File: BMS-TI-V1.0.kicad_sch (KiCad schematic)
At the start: 0 parts

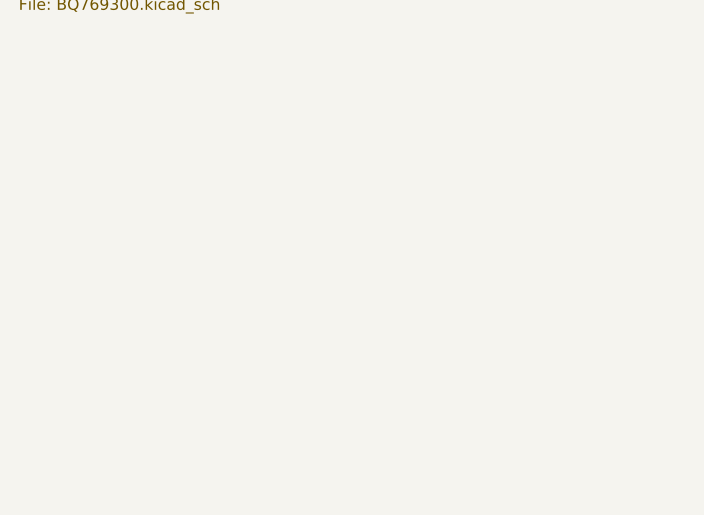
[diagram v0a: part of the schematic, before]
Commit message: Added BQ78350 Gas-gauge companion
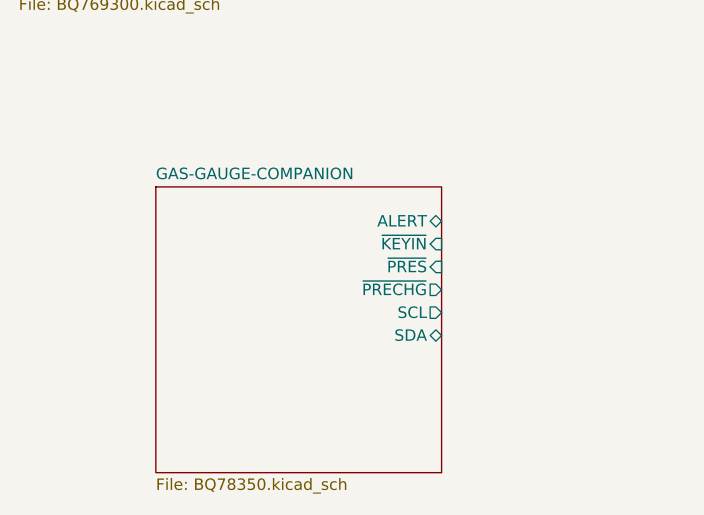
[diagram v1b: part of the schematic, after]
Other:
- added sheet GAS-GAUGE-COMPANION (BQ78350.kicad_sch)
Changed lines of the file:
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@@
+		)
+	)
+	(sheet
+		(at 120.65 129.54)
+		(size 31.75 31.75)
+		(fields_autoplaced yes)
+		(stroke
+			(width 0.1524)
+			(type solid)
+		)
+		(fill
+			(color 0 0 0 0.0000)
+		)
+		(property "Sheetname" "GAS-GAUGE-COMPANION"
+			(at 120.65 128.8284 0)
+			(effects
+				(font
+					(size 1.27 1.27)
+				)
+				(justify left bottom)
+			)
+		)
+		(property "Sheetfile" "BQ78350.kicad_sch"
+			(at 120.65 161.8746 0)
+			(effects
+				(font
+					(size 1.27 1.27)
+				)
+				(justify left top)
+			)
+		)
+		(pin "ALERT" bidirectional
+			(at 152.4 133.35 0)
+			(effects
+				(font
+					(size 1.27 1.27)
+				)
+				(justify right)
+			)
+		)
+		(pin "~{KEYIN}" input
+			(at 152.4 135.89 0)
+			(effects
+				(font
+					(size 1.27 1.27)
+				)
+				(justify right)
+			)
+		)
+		(pin "~{PRES}" input
+			(at 152.4 138.43 0)
+			(effects
+				(font
+					(size 1.27 1.27)
+				)
+				(justify right)
+			)
+		)
+		(pin "~{PRECHG}" output
+			(at 152.4 140.97 0)
+			(effects
+				(font
+					(size 1.27 1.27)
+				)
+				(justify right)
+			)
+		)
+		(pin "SCL" output
+			(at 152.4 143.51 0)
+			(effects
+				(font
+					(size 1.27 1.27)
+				)
+				(justify right)
+			)
+		)
+		(pin "SDA" bidirectional
+			(at 152.4 146.05 0)
+			(effects
+				(font
+					(size 1.27 1.27)
+				)
+				(justify right)
+			)
+		)
+		(instances
+			(project "BMS-TI-V1.0"
+				(path "/1b322c88-a1e6-4706-b5ad-2d81e9035abf"
+					(page "4")
+				)
+			)
 		)
 	)

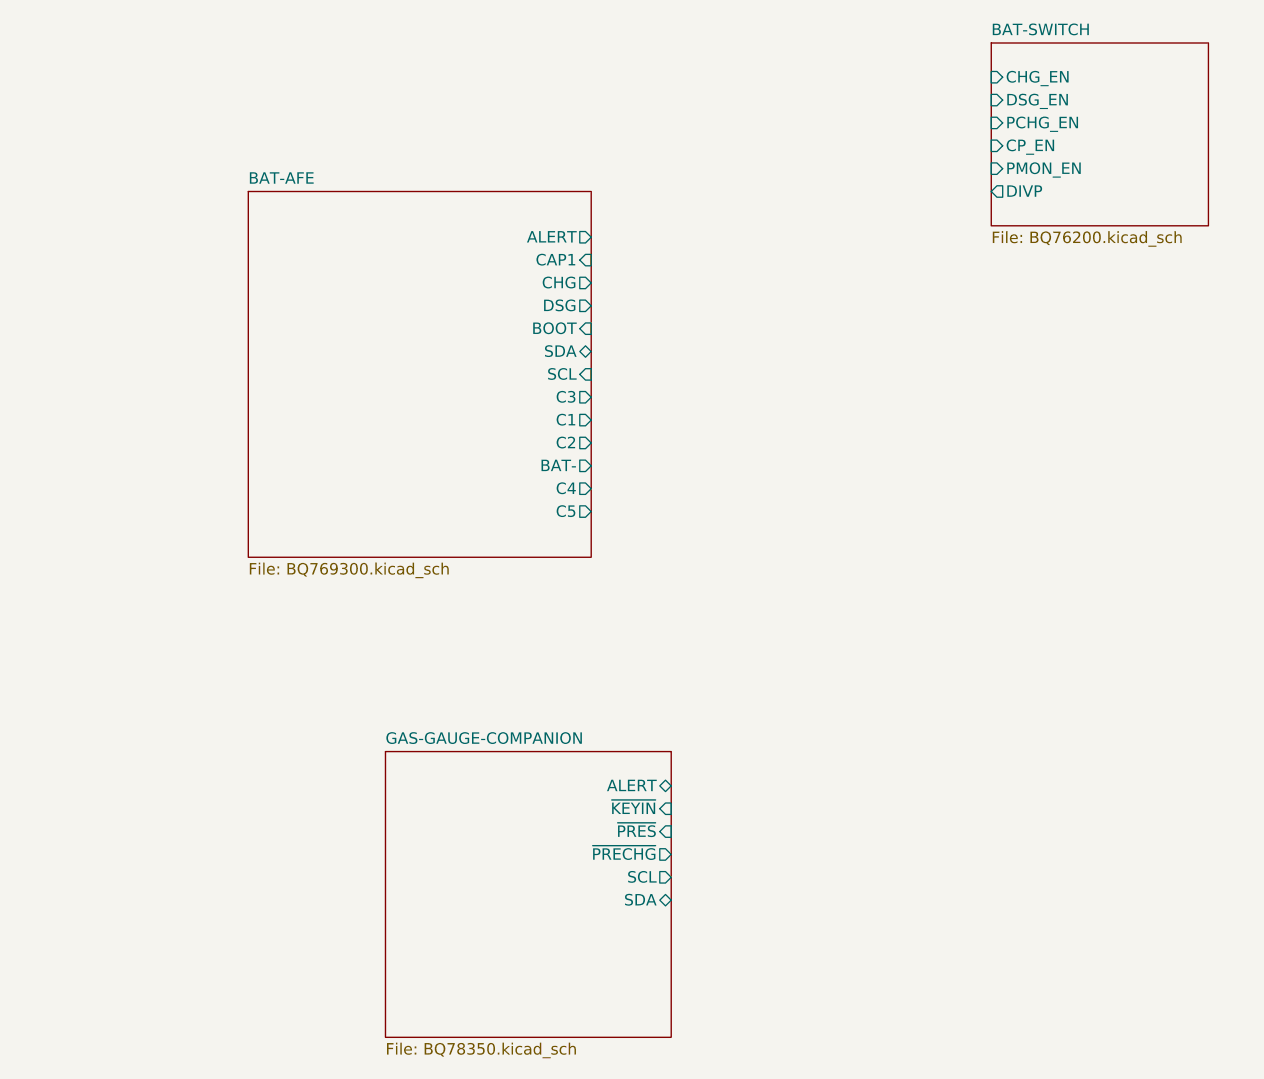
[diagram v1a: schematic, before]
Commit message: Changes Mosfet's package to D2PAK
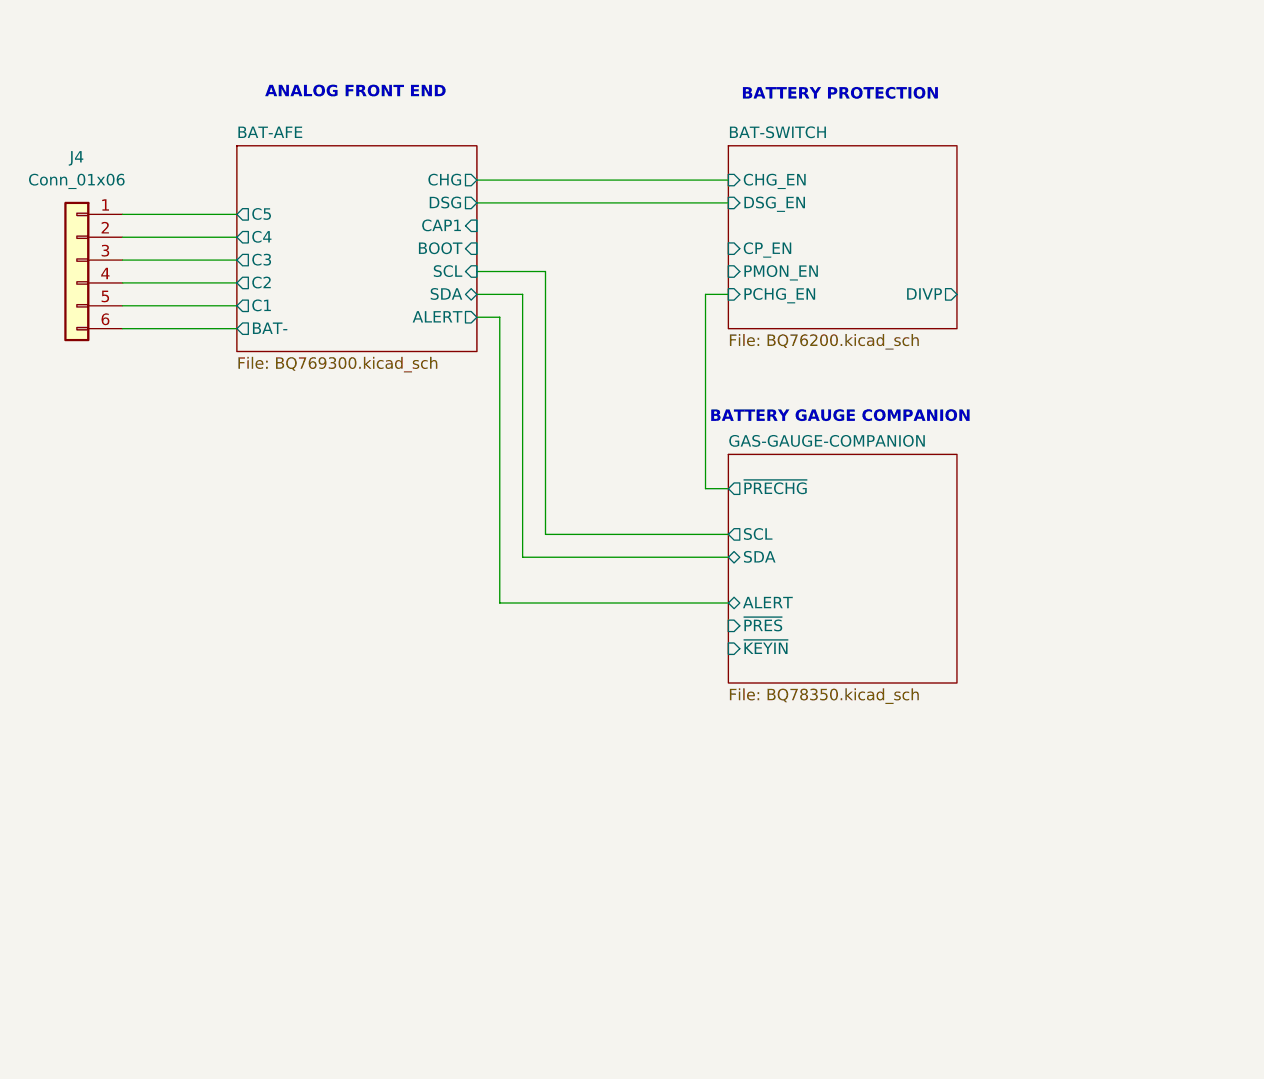
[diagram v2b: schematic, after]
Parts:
- added J4: Conn_01x06, Connector_JST:JST_XH_B6B-XH-A_1x06_P2.50mm_Vertical, symbol Connector_Generic:Conn_01x06
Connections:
- net BAT-AFE/BAT-: now also J4.6 (Pin_6)
- net BAT-AFE/C1: now also J4.5 (Pin_5)
- net BAT-AFE/C2: now also J4.4 (Pin_4)
- net BAT-AFE/C3: now also J4.3 (Pin_3)
- net BAT-AFE/C4: now also J4.2 (Pin_2)
- net BAT-AFE/C5: now also J4.1 (Pin_1)
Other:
- note added: "ANALOG FRONT END"
- note added: "BATTERY GAUGE COMPANION"
- note added: "BATTERY PROTECTION"
